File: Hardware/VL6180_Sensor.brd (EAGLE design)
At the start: 44.5 x 13 mm, 24 parts, among them U1 VL6180, U3 MIC5219 3.3V

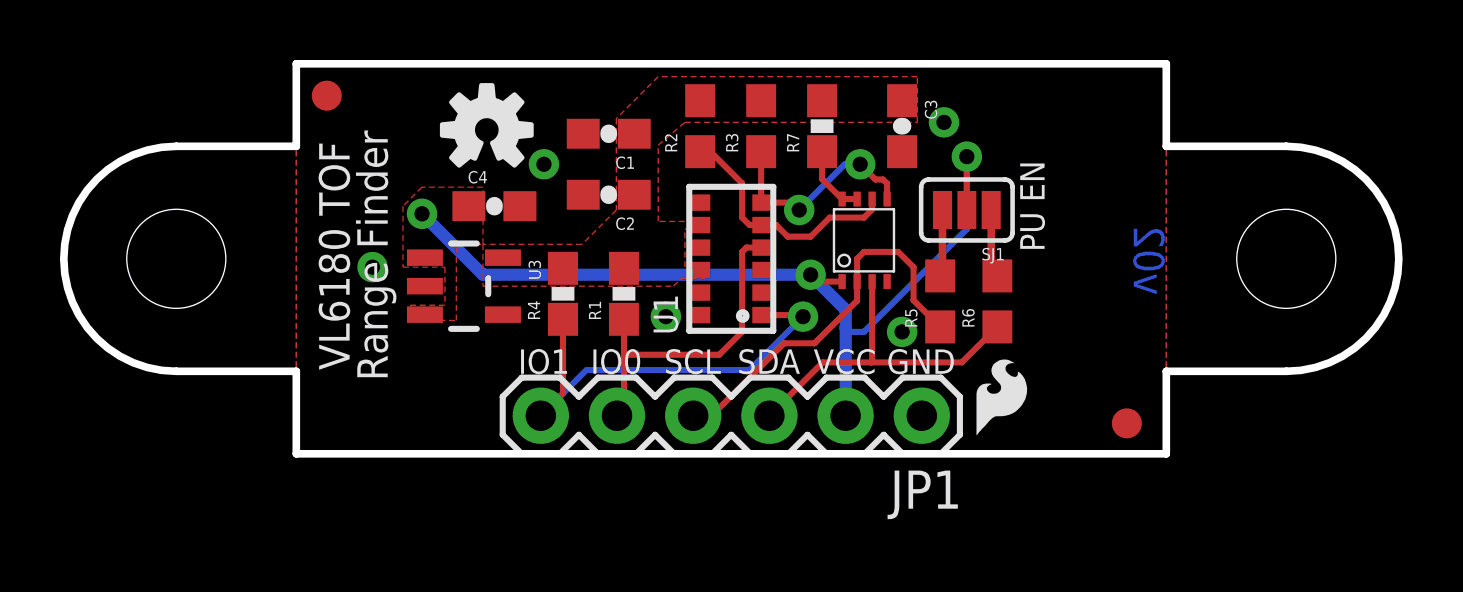
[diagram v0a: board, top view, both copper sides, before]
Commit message: modified:   Hardware/VL6180_Breakout.brd 	modified:   Hardware/VL6180_Breakout.sch 	renamed:    Hardware/VL6180.brd -> Hardware/VL6180_Sensor.brd 	renamed:    Hardware/VL6180.sch -> Hardware/VL6180_Sensor.sch
Removed I2C level shifter and switched to Fet bases solution.
New solderpaste footprint for VL6180 for improved reflow.
updated all parts with Sparkle ID's
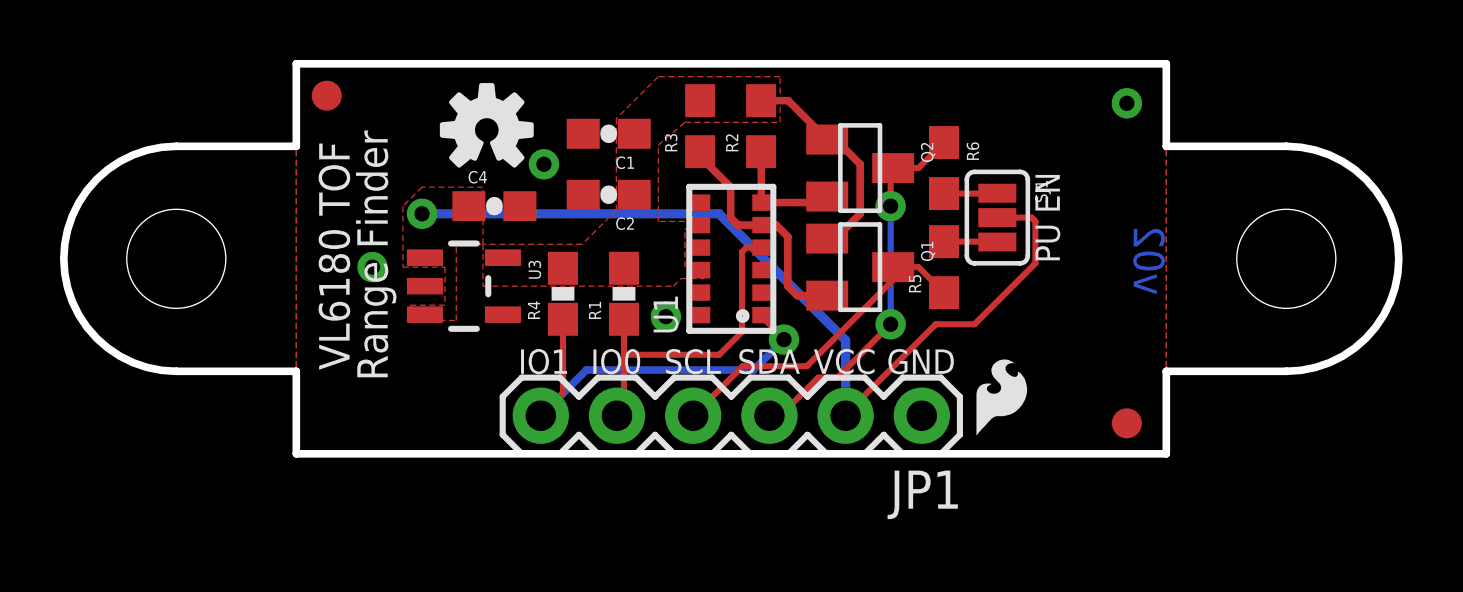
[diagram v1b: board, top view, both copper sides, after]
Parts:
- removed C3: 0.1uF, SparkFun-Capacitors:0603-CAP
- removed R7: 200k, SparkFun-Resistors:0603-RES
- removed U2: (no value), SparkFun-DigitalIC:PSOP-8
- added Q1, Q2: BSS138, SparkFun-DiscreteSemi:SOT23
- moved R6 4.79 mm to (21.6, 9.53), turned to 270 degrees
- moved R2 2.03 mm to (15.5, 10.9)
- moved R3 2.03 mm to (13.5, 10.9)
- moved R5 1.15 mm to (21.6, 6.22)
- moved SJ1 1.05 mm to (23.4, 7.87), turned to 270 degrees
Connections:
- removed net N$1: R7.1, U2.7, U2.8
- net 2.8V: now also Q1.1, Q2.1; no longer C3.1, R7.2
- net GND: no longer C3.2, U2.4
- net SCL: now also Q1.3; no longer U2.2
- net SCL_LV: now also Q1.2, R3.1; no longer R2.1, U2.6
- net SDA: now also Q2.3; no longer U2.3
- net SDA_LV: now also Q2.2, R2.1; no longer R3.1, U2.5
- net VCC: no longer U2.1
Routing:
- net 2.8V: track 0.00 -> 7.27 mm
- net SDA_LV: track 7.41 -> 4.10 mm, vias 2 -> 0
- net N$1: track 2.36 -> 0.00 mm
- net SCL: track 13.0 -> 11.0 mm
- net GPIO1: track 15.0 -> 13.8 mm
- net SDA: track 11.5 -> 12.6 mm, vias 0 -> 2
- net VCC: track 29.8 -> 29.5 mm, vias 3 -> 1

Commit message: changed I2C resistors to 2.2k, added current limiting resistor on GPIO pins.
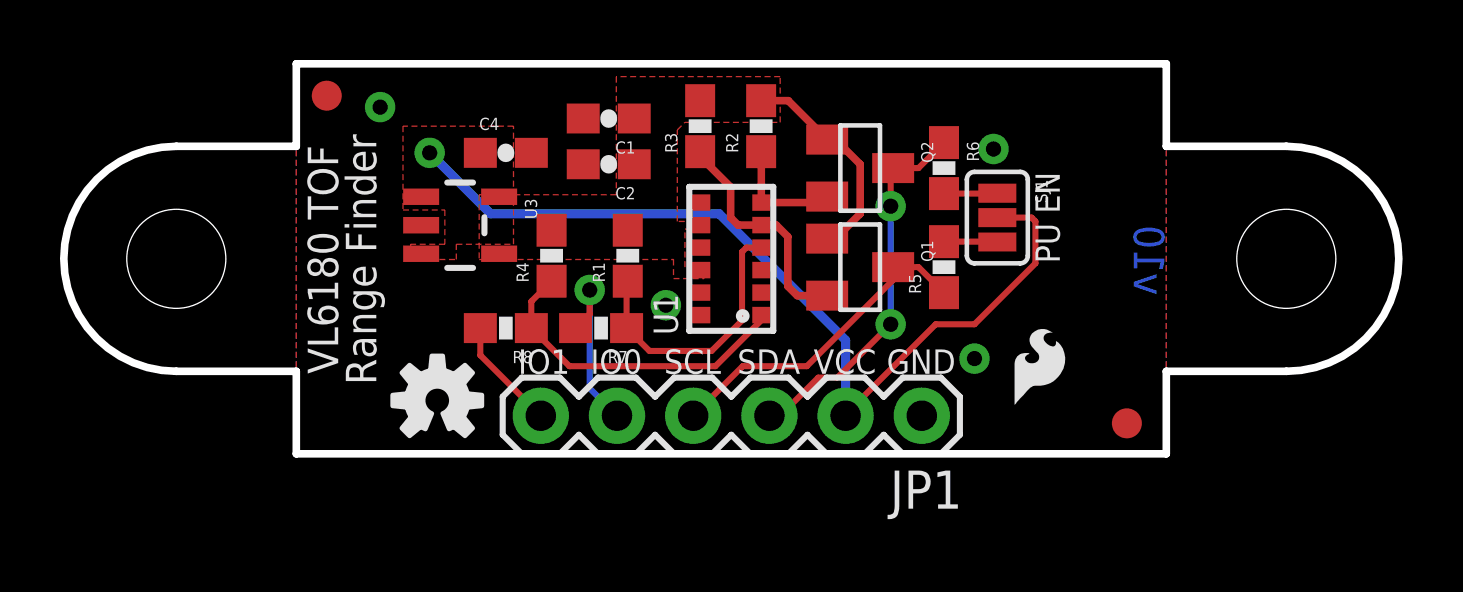
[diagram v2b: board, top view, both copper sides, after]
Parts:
- added R7, R8: 10k, SparkFun-Resistors:0603-RES
- R1, R4: value 10K -> 47k
- R2, R3, R5, R6: value 4.7k -> 2.2k; device SparkFun-Resistors:0603 -> SparkFun-Resistors:0603-RES
- SJ1: device SparkFun-Passives:SJ_3_PASTE1&2&3 -> SparkFun-Passives:PAD-JUMPER-3-NC_BY_PASTE_YES_SILK_FULL_BOX
- moved LOGO2 9.17 mm to (4.70, 1.78)
- moved U3 2.04 mm to (5.46, 7.62)
- moved C4 1.82 mm to (6.99, 10.0)
- moved U$2 1.63 mm to (23.6, 1.27)
- moved R4 1.33 mm to (8.51, 6.60)
- moved R1 1.28 mm to (11.0, 6.60)
- moved C2 1.02 mm to (10.4, 9.65)
- moved C1 0.51 mm to (10.4, 11.2)
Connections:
- new net N$100: R1.1, R7.1, U1.4
- new net N$103: R4.1, R8.1, U1.1
- net GPIO0: now also R7.2; no longer R1.1, U1.4
- net GPIO1: now also R8.2; no longer R4.1, U1.1
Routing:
- net N$103: track 0.00 -> 10.8 mm
- net GPIO1: track 13.8 -> 3.76 mm, vias 1 -> 0
- net N$100: track 0.00 -> 9.14 mm
- net GPIO0: track 10.9 -> 6.03 mm, vias 0 -> 1
- net VCC: track 29.5 -> 30.2 mm
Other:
- board text added: "v10"
- board text removed: "v02"
